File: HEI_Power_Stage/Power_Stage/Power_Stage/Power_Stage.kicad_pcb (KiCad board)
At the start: 4 copper layers, 100 x 56 mm, 130 parts, among them J1 OSTTA020161, J2 Conn_02x10_Odd_Even, J3 Screw_Terminal_01x01, J4 Screw_Terminal_01x01, J5 Screw_Terminal_01x01, Q1 EPC2304ENGRT, Q2 EPC2304ENGRT, Q3 EPC2304ENGRT, Q4 EPC2304ENGRT, Q5 EPC2304ENGRT, Q6 EPC2304ENGRT, T1 30k, T2 30k, T3 30k, T4 30k, T5 30k, T6 30k, U1 TBA 2-1212, U11 NCP51820AMNTWG, U12 ADC124S051CIMM/NOPB, U2 1769205241, U3 TPS73250DBVR, U5 NCP51820AMNTWG, U6 ADC124S051CIMM/NOPB, U8 NCP51820AMNTWG, U9 ADC124S051CIMM/NOPB

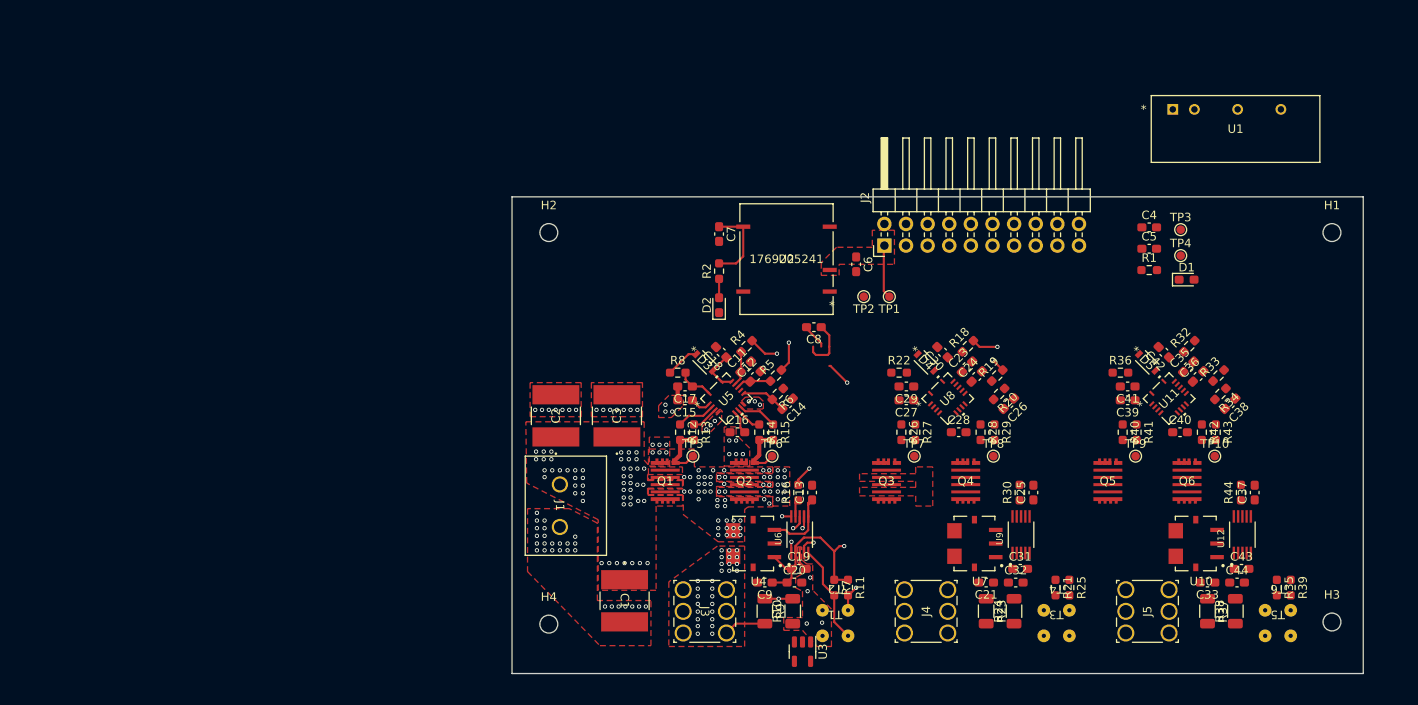
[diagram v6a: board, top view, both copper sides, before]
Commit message: layout
5v regulators for each phase daq
12v iso
top half and bottom half planes
SPi goes from bottom to top layer at plane split
power routed on bottom two layers with solid planes
switch nodes on top two layers
4 adcs now
daq for dc input
current sensors now references to gndpwr
Still need to figure out how to connect gndpwr pours with isolation
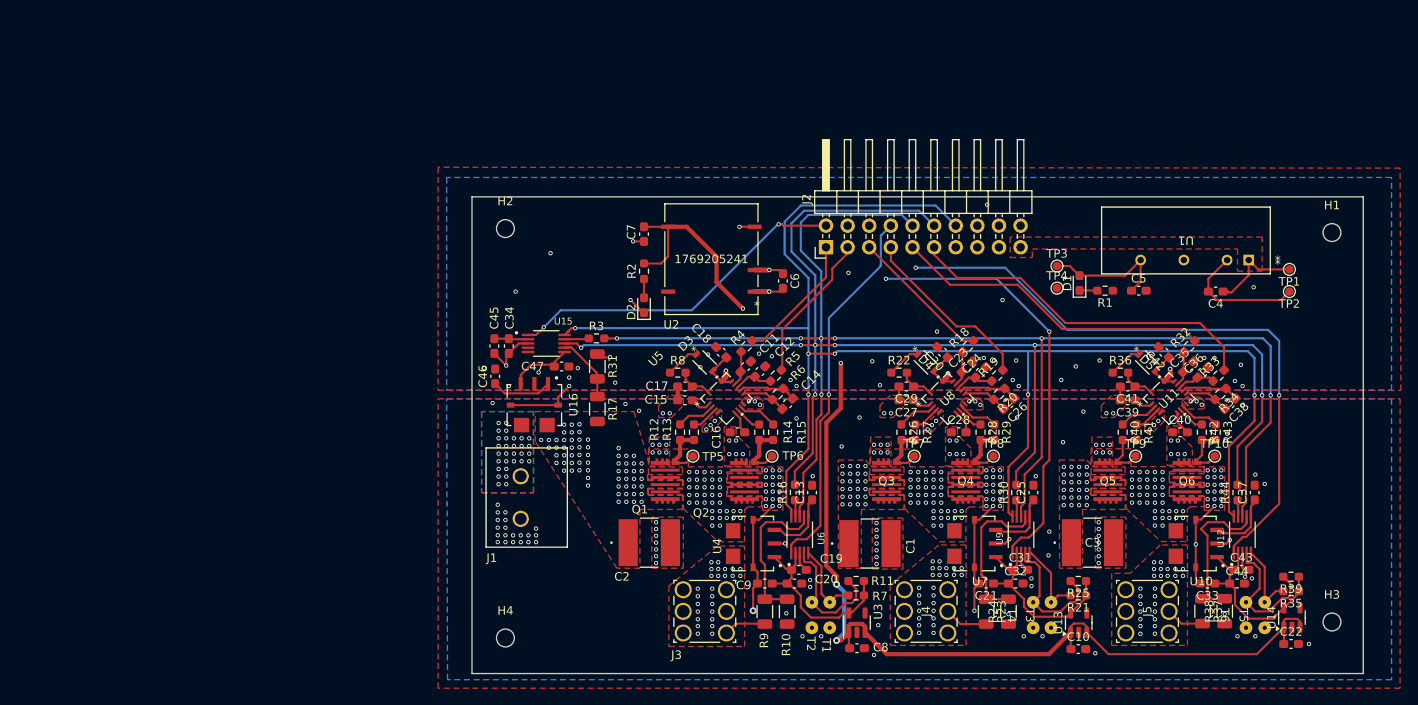
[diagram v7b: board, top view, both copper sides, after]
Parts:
- added C10: 10uF, Capacitor_SMD:C_0603_1608Metric_Pad1.08x0.95mm_HandSolder, F.Cu at (158.2, 154.4)
- added C22: 10uF, Capacitor_SMD:C_0603_1608Metric_Pad1.08x0.95mm_HandSolder, F.Cu at (183.2, 153.8)
- added C34: 0.1uF, Capacitor_SMD:C_0603_1608Metric_Pad1.08x0.95mm_HandSolder, F.Cu at (91.3, 118.8)
- added C45: 1uF, Capacitor_SMD:C_0603_1608Metric_Pad1.08x0.95mm_HandSolder, F.Cu at (89.6, 118.8)
- added C46: 0.1uF, Capacitor_SMD:C_0603_1608Metric_Pad1.08x0.95mm_HandSolder, F.Cu at (89.7, 122.4)
- added C47: 1nF, Capacitor_SMD:C_0603_1608Metric_Pad1.08x0.95mm_HandSolder, F.Cu at (97.5, 121.2)
- added R17: 715k, Resistor_SMD:R_1206_3216Metric, F.Cu at (101.7, 126.2)
- added R3: 330, Resistor_SMD:R_0603_1608Metric_Pad0.98x0.95mm_HandSolder, F.Cu at (101.6, 117.9)
- added R31: 10k, Resistor_SMD:R_1206_3216Metric, F.Cu at (101.7, 121.2)
- added U13: TPS73250DBVR, Package_TO_SOT_SMD:TSOT-23-5, F.Cu at (158.2, 151.3)
- added U14: TPS73250DBVR, Package_TO_SOT_SMD:TSOT-23-5, F.Cu at (183.3, 150.7)
- added U15: ADC124S051CIMM/NOPB, GTSR:SOP50P490X110-10N, F.Cu at (95.7, 118.5)
- added U16: ~, GTSR:XDCR_ACS72981LLRATR-100B5, F.Cu at (94.3, 125.7)
- moved C3 57.8 mm to (159.9, 141.9), turned to 0 degrees
- moved TP2 50.0 mm to (183.0, 112.4)
- moved TP1 47.1 mm to (183.0, 109.8)
- moved C8 38.1 mm to (132.2, 154.3), turned to 0 degrees
- moved C1 29.6 mm to (133.7, 142.0), turned to 0 degrees
- moved U1 19.8 mm to (178.2, 108.7), turned to 180 degrees
- moved C2 18.5 mm to (107.8, 141.9), turned to 0 degrees
- moved TP3 15.1 mm to (155.7, 109.4)
- moved TP4 15.0 mm to (155.7, 112.0)
- moved D1 12.6 mm to (158.3, 111.4), turned to 90 degrees
- moved C4 10.9 mm to (174.3, 112.4), turned to 180 degrees
- moved C6 8.82 mm to (123.5, 111.2)
- moved U2 8.82 mm to (115.1, 108.6)
- moved C7 8.82 mm to (107.2, 105.7)
- moved D2 8.82 mm to (107.2, 114.0)
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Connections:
- C13 pad 2: GND -> GNDPWR
- C19 pad 1: /5Vref -> /5VrefA
- C20 pad 1: /5Vref -> /5VrefA
- C21 pad 1: /5Vref -> /5VrefB
- C21 pad 2: GND -> GNDPWR
- C25 pad 2: GND -> GNDPWR
- C31 pad 1: /5Vref -> /5VrefB
- C32 pad 1: /5Vref -> /5VrefB
- C33 pad 1: /5Vref -> /5VrefC
- C33 pad 2: GND -> GNDPWR
- C37 pad 2: GND -> GNDPWR
- C4 pad 1: +12V -> +12V_LV
- C43 pad 1: /5Vref -> /5VrefC
- C44 pad 1: /5Vref -> /5VrefC
- C6 pad 1: +12V -> +12V_LV
- C9 pad 1: /5Vref -> /5VrefA
- C9 pad 2: GND -> GNDPWR
- J1 pad 1: VDC -> VDCin
- J2 pad 1: /CHS_{PWM} -> /AHS_{PWM}
- J2 pad 11: /ALS_{PWM} -> /CLS_{PWM}
- J2 pad 19: +12V -> +12V_LV
- J2 pad 2: unconnected-(J2-Pin_2-Pad2) -> /DC~{CS}
- J2 pad 3: /CLS_{PWM} -> /ALS_{PWM}
- J2 pad 9: /AHS_{PWM} -> /CHS_{PWM}
- R11 pad 1: /5Vref -> /5VrefA
- R21 pad 1: /5Vref -> /5VrefB
- R25 pad 1: /5Vref -> /5VrefB
- R35 pad 1: /5Vref -> /5VrefC
- R39 pad 1: /5Vref -> /5VrefC
- R7 pad 1: /5Vref -> /5VrefA
- TP1 pad 1: +12V -> +12V_LV
- U1 pad 1: +12V -> +12V_LV
- U10 pad 1: /5Vref -> /5VrefC
- U10 pad 2: GND -> GNDPWR
- U10 pad 4: GND -> GNDPWR
- U10 pad 7: GND -> GNDPWR
- U12 pad 2: /5Vref -> /5VrefC
- U2 pad 2: +12V -> +12V_LV
- U3 pad 5: /5Vref -> /5VrefA
- U4 pad 1: /5Vref -> /5VrefA
- U4 pad 2: GND -> GNDPWR
- U4 pad 4: GND -> GNDPWR
- U4 pad 7: GND -> GNDPWR
- U6 pad 2: /5Vref -> /5VrefA
- U7 pad 1: /5Vref -> /5VrefB
- U7 pad 2: GND -> GNDPWR
- U7 pad 4: GND -> GNDPWR
- U7 pad 7: GND -> GNDPWR
- U9 pad 2: /5Vref -> /5VrefB
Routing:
- net /CLK: track 1.08 -> 181.7 mm, vias 1 -> 6
- net /MOSI: track 1.83 -> 172.6 mm, vias 1 -> 7
- net /MISO: track 2.44 -> 167.5 mm, vias 1 -> 7
- net +5V: track 15.7 -> 180.8 mm, vias 0 -> 4
- net +12V: track 11.9 -> 103.6 mm, vias 0 -> 3
- net /C~{CS}: track 0.00 -> 87.0 mm, vias 0 -> 2
- net GNDPWR: track 5.37 -> 63.9 mm, vias 73 -> 174
- net /B~{CS}: track 0.00 -> 57.3 mm, vias 0 -> 2
- net /GND_LV: track 0.00 -> 56.3 mm, vias 0 -> 1
- net +12V_LV: track 0.00 -> 47.5 mm, vias 0 -> 1
- net /A~{CS}: track 1.33 -> 44.0 mm
- net /CLS_{PWM}: track 0.00 -> 42.1 mm
- net /DC~{CS}: track 0.00 -> 40.5 mm, vias 0 -> 2
- net /CHS_{PWM}: track 0.00 -> 37.7 mm
- net /5VrefA: track 0.00 -> 30.1 mm
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- added copper zone on F.Cu, net +12V_LV
- added copper zone on In1.Cu, net /GND_LV
- added copper zone on F.Cu, net /PHB
- added copper zone on In1.Cu, net /PHB
- added copper zone on F.Cu, net /PHC
- added copper zone on In1.Cu, net /PHC
- added copper zone on F.Cu, net /Phase2/SW
- added copper zone on In1.Cu, net /Phase2/SW
- added copper zone on F.Cu, net /Phase3/SW
- added copper zone on In1.Cu, net /Phase3/SW
- added copper zone on F.Cu, net GND
- added copper zone on In1.Cu, net GND
- added copper zone on B.Cu, net GNDPWR
- added copper zone on In2.Cu, net GNDPWR
- added copper zone on B.Cu, net VDC
- added copper zone on B.Cu, net VDCin
- added copper zone on F.Cu, net VDCin
- removed copper zone on F.Cu, net +12V
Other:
- board size 100 x 56 mm -> 104.7 x 56 mm
- board text added: "Fill Pours Top half: gnd gnd pwrgnd pwrgnd -------- Bottom half: pwrgnd pwrgnd pwrgnd vdc"

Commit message: changes since class on friday
solid gndpwr plane on layer 3
new cap... its large
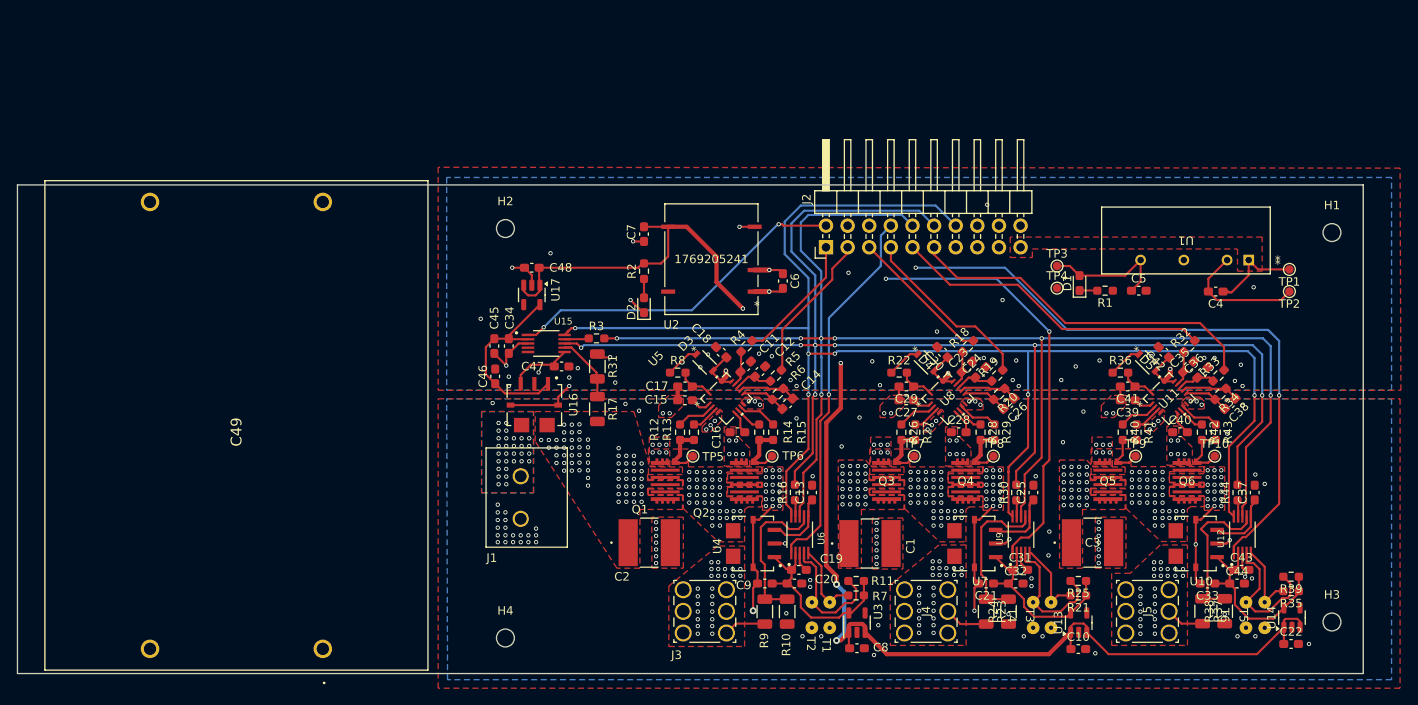
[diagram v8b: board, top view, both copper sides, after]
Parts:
- added C48: 10uF, Capacitor_SMD:C_0603_1608Metric_Pad1.08x0.95mm_HandSolder, F.Cu at (94.0, 109.6)
- added C49: 210uF, kemet_cap:C4AQLEW6210A3BK, F.Cu at (69.5, 154.4)
- added U17: TPS73250DBVR, Package_TO_SOT_SMD:TSOT-23-5, F.Cu at (94.0, 112.8)
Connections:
- C34 pad 1: /5V -> /5VrefDC
- C45 pad 1: /5V -> /5VrefDC
- C46 pad 1: /5VrefA -> /5VrefDC
- U15 pad 2: /5V -> /5VrefDC
- U16 pad 1: /5VrefA -> /5VrefDC
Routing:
- net /5VrefDC: track 0.00 -> 22.8 mm
- net +5V: track 180.8 -> 199.1 mm
- net /5VrefA: track 30.1 -> 23.0 mm
- net /5V: track 3.98 -> 0.00 mm
- net GNDPWR: track 63.9 -> 67.8 mm, vias 174 -> 175
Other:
- board size 104.7 x 56 mm -> 158.1 x 57.4 mm
